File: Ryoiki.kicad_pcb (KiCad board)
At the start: 2 copper layers, 15 x 35.7 mm, 46 parts, among them J1 USB_C_Receptacle, J2 Conn_02x06, SW1 bootsel, SW2 restart, U1 W25Q32JVSS, U2 TLV74333PDBVR, U3 RP2040, Y1 12Mhz

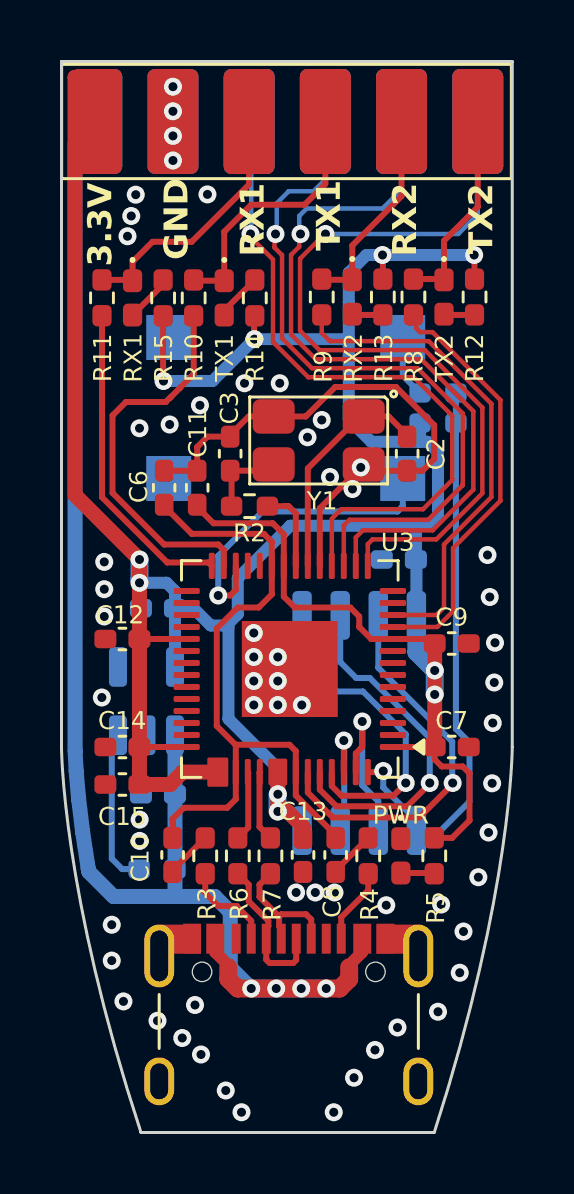
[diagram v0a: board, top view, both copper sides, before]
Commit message: - Added ESD protection (USBLC6-2SC6) to the USB data lines and VBUS. - add more satoru gojo
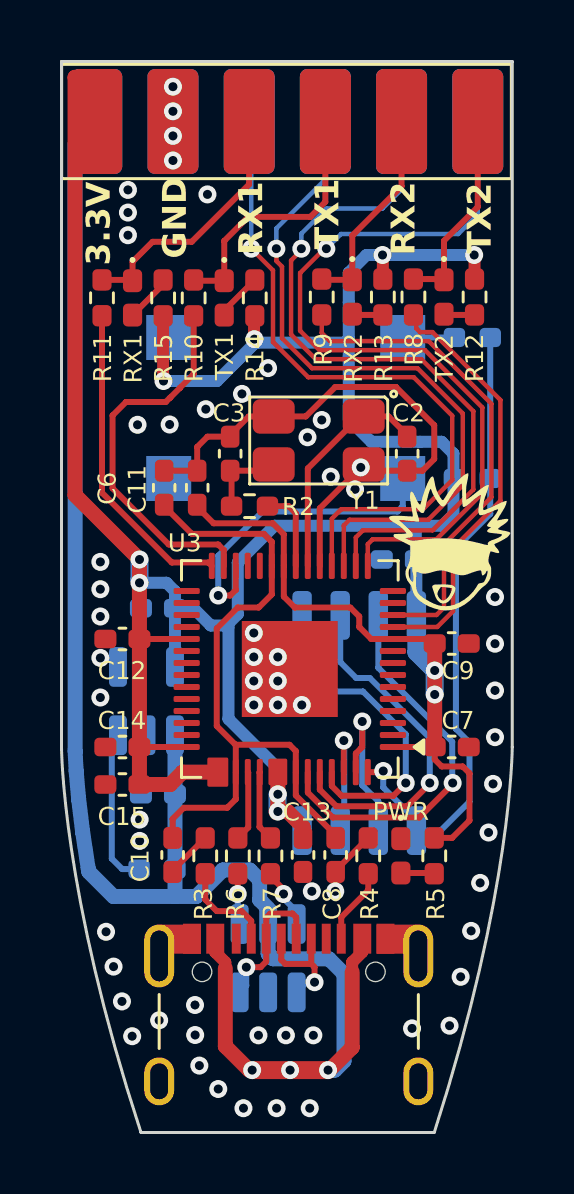
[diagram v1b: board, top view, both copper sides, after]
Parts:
- removed the G*** at (153.8, 136.8)
- added G***: LOGO, LOGO, F.Cu at (159.2, 120.6)
- added G***: LOGO, LOGO, B.Cu at (156.3, 138.2)
- added U4: USBLC6-2SC6, Package_TO_SOT_SMD:SOT-23-6, B.Cu at (153.1, 134.5)
- moved R16 2.18 mm to (159.9, 113.8)
- moved R17 2.18 mm to (159.9, 118.5)
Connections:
- J1 pad A6: /USB_D+ -> Net-(J1-D+-PadA6)
- J1 pad A7: /USB_D- -> Net-(J1-D--PadA7)
- J1 pad B6: /USB_D+ -> Net-(J1-D+-PadA6)
- J1 pad B7: /USB_D- -> Net-(J1-D--PadA7)
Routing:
- net VBUS: track 47.2 -> 59.5 mm, vias 4 -> 3
- net Net-(J1-D--PadA7): track 0.00 -> 5.08 mm, vias 0 -> 1
- net Net-(J1-D+-PadA6): track 0.00 -> 4.14 mm, vias 0 -> 1
- net /USB_D-: track 5.11 -> 1.70 mm, vias 0 -> 1
- net /QSPI_SS: track 19.0 -> 21.3 mm
- net /USB_D+: track 4.43 -> 2.48 mm, vias 0 -> 1
- net +3.3V: track 111.9 -> 112.7 mm

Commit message: update gojo icons
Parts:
- removed the G*** at (159.2, 120.6)
- removed the G*** at (156.3, 138.2)
- added G***: LOGO, LOGO, F.Cu at (159.1, 120.4)
- added G***: LOGO, LOGO, B.Cu at (152.4, 129.6)
